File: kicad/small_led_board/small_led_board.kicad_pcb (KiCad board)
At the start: 2 copper layers, 137.2 x 99.1 mm, 107 parts, among them J1 Breakout to FPGA, J2 +5V IN, Q1 IRLZ44N, Q10 IRF4905, Q11 IRF4905, Q12 IRF4905, Q13 IRF4905, Q14 IRF4905, Q15 IRLZ44N, Q16 IRLZ44N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

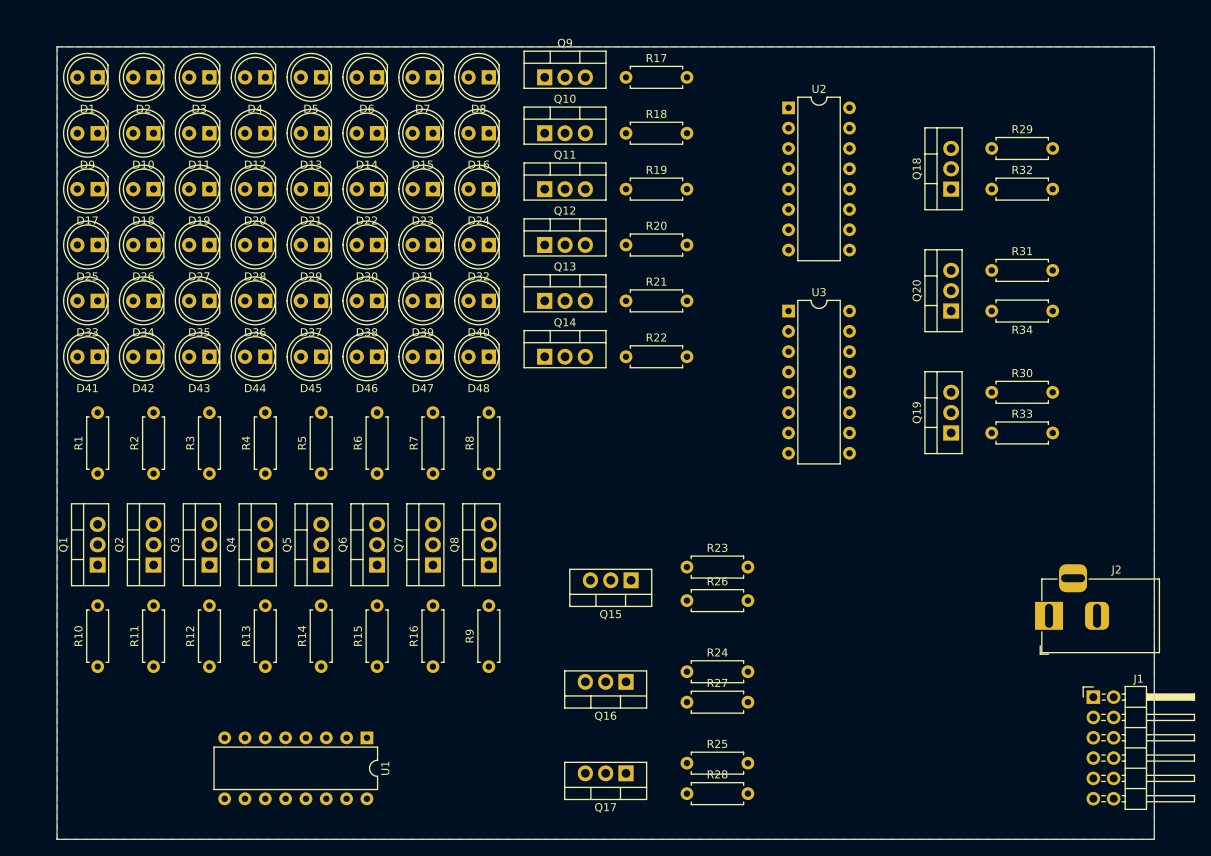
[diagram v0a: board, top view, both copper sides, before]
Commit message: small_led_board: Placed and Routed PCB
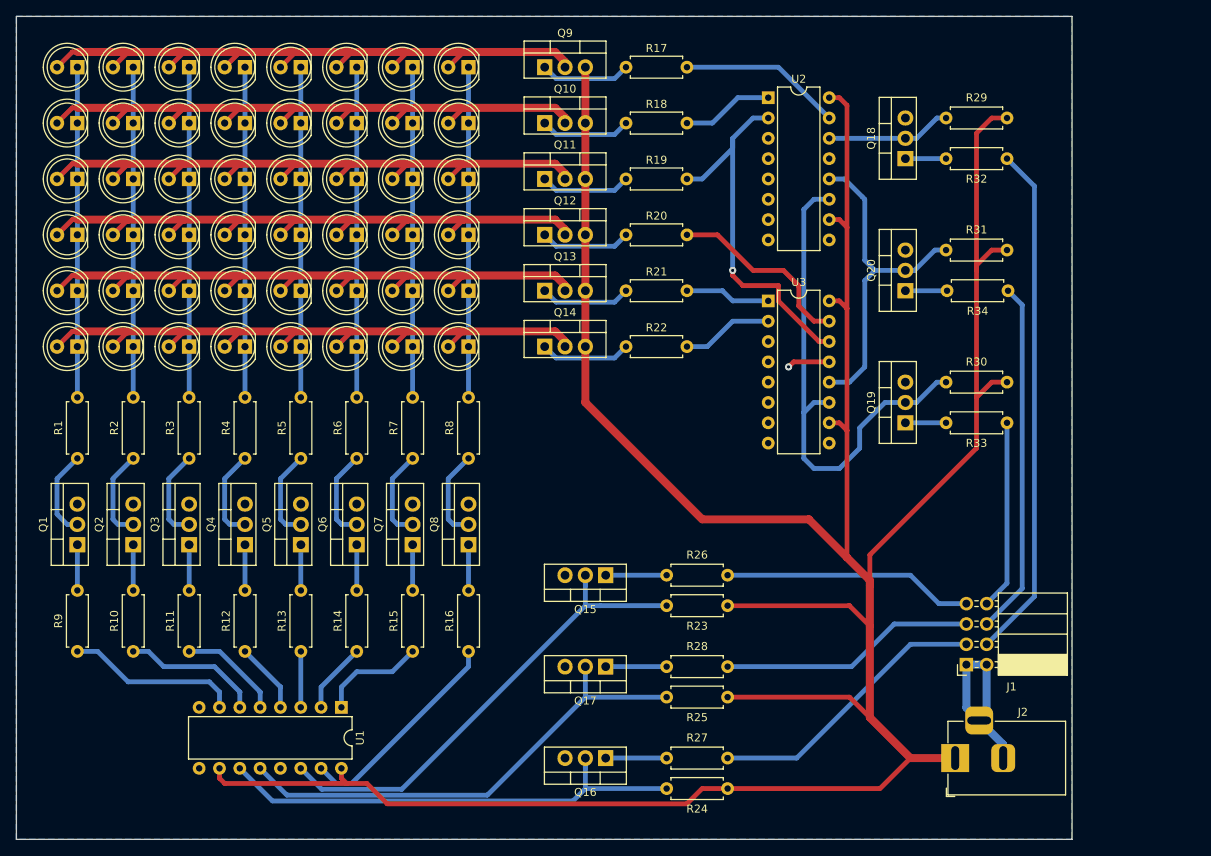
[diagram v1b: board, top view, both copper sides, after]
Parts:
- J1: value Breakout to FPGA -> TO FPGA; footprint Connector_PinHeader_2.54mm:PinHeader_2x06_P2.54mm_Horizontal -> Connector_PinSocket_2.54mm:PinSocket_2x04_P2.54mm_Horizontal
- moved R9 51.5 mm to (68.6, 116.2)
- moved J2 21.3 mm to (178.3, 129.5)
- moved J1 16.4 mm to (179.7, 117.9), turned to 180 degrees
- moved R28 16.1 mm to (142.2, 118.1)
- moved R24 14.8 mm to (142.2, 133.3)
- moved Q17 13.6 mm to (134.6, 118.1)
- moved R34 13.5 mm to (177.3, 71.1), turned to 0 degrees
- moved Q16 9.86 mm to (134.6, 129.5)
- moved R25 8.64 mm to (142.2, 121.9)
- moved R27 7.43 mm to (142.2, 129.5)
- moved Q18 6.87 mm to (172.1, 54.6)
- moved R29 6.87 mm to (177.2, 49.5)
- moved R32 6.87 mm to (177.2, 54.6)
- moved Q20 6.25 mm to (172.1, 71.1)
- moved R31 6.25 mm to (177.2, 66.0)
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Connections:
- J1 pad 1: FPGA_GND -> GND
- J1 pad 2: RowDataIn_n -> GND
- J1 pad 4: ApplyNewRow_n -> RowStrobeIn_n
- J1 pad 5: ApplyNewRowStrobe_n -> ApplyNewRow_n
- J1 pad 6: RowStrobeAdvance_n -> ApplyNewRowStrobe_n
- J1 pad 7: RowStrobeIn_n -> RowDataIn_n
- J1 pad 8: FPGA_GND -> RowStrobeAdvance_n
- J2 pad 1: GND -> +5V
- J2 pad 2: +5V -> GND
- J2 pad 3: (no net) -> GND
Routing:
- net +5V: track 0.00 -> 391.2 mm
- net Net-(D10-A): track 0.00 -> 84.4 mm
- net Net-(D33-A): track 0.00 -> 84.3 mm
- net Net-(D1-A): track 0.00 -> 84.3 mm
- net Net-(D17-A): track 0.00 -> 84.3 mm
- net Net-(D25-A): track 0.00 -> 84.3 mm
- net Net-(D41-A): track 0.00 -> 84.3 mm
- net RowStrobeIn_n: track 0.00 -> 64.6 mm
- net Net-(Q19-D): track 0.00 -> 62.8 mm
- net Net-(Q15-D): track 0.00 -> 61.4 mm
- net Net-(Q17-D): track 0.00 -> 61.1 mm
- net Net-(Q16-D): track 0.00 -> 60.8 mm
- net Net-(U2-QC): track 0.00 -> 47.8 mm, vias 0 -> 1
- net ApplyNewRowStrobe_n: track 0.00 -> 44.2 mm
- net Net-(Q20-D): track 0.00 -> 42.7 mm
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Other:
- board size 137.2 x 99.1 mm -> 132 x 102.9 mm
- copper layers 2 -> 4

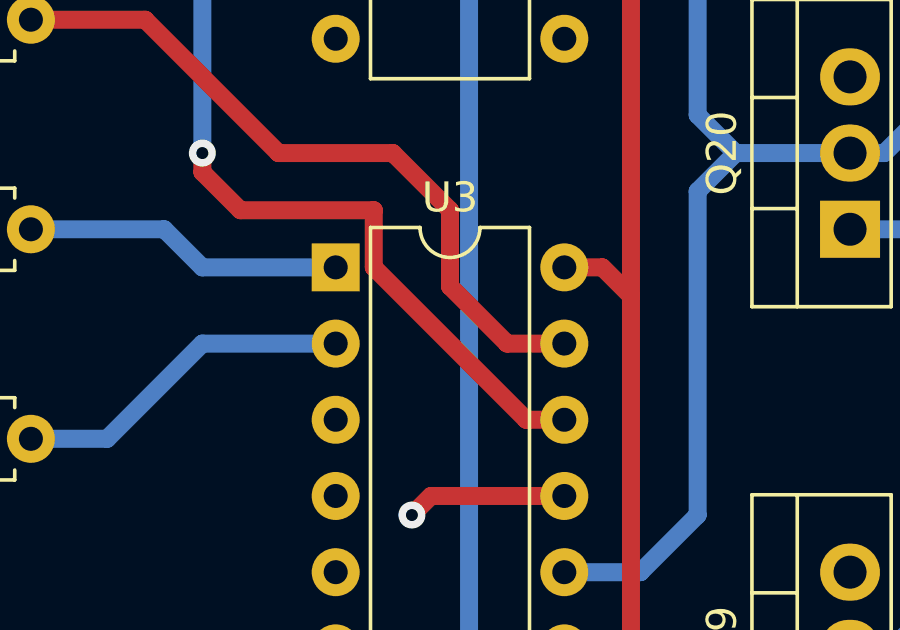
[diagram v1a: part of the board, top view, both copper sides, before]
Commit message: small_led_board: Changed PCB settings
Constraints were originally pulled from a git template project.
Changed 4 layers to 2 layers as only Front and Back are needed.
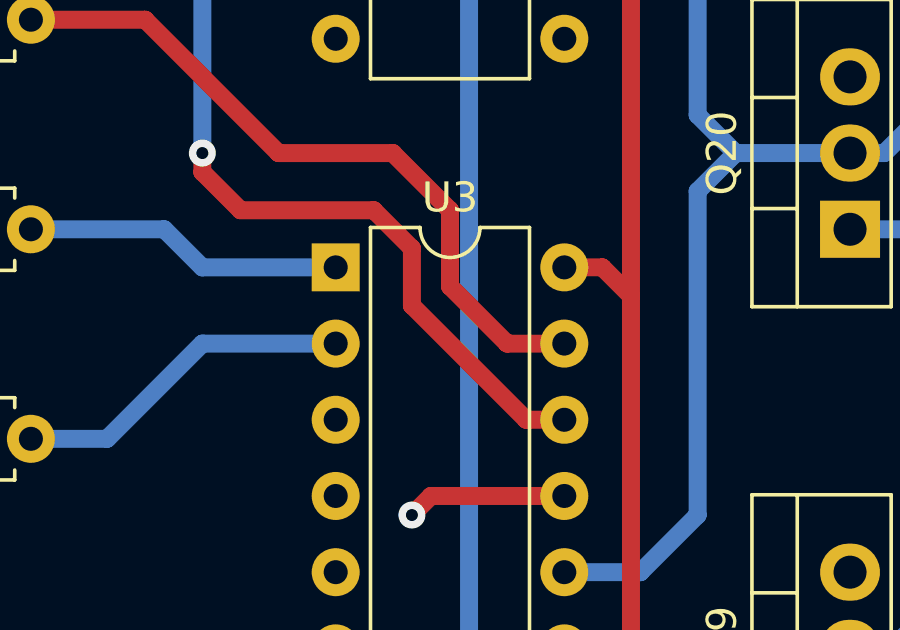
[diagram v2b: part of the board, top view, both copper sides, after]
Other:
- copper layers 4 -> 2
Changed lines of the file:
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@@
   (layers
     (0 "F.Cu" signal "Front")
-    (1 "In1.Cu" signal)
-    (2 "In2.Cu" signal)
     (31 "B.Cu" signal "Back")
     (34 "B.Paste" user)
@@
       (layer "F.Mask" (type "Top Solder Mask") (thickness 0.01))
       (layer "F.Cu" (type "copper") (thickness 0.035))
-      (layer "dielectric 1" (type "core") (thickness 1.51) (material "FR4") (epsilon_r 4.5) (loss_tangent 0.02))
-      (layer "In1.Cu" (type "copper") (thickness 0.035))
-      (layer "dielectric 2" (type "prepreg") (thickness 1.51) (material "FR4") (epsilon_r 4.5) (loss_tangent 0.02))
-      (layer "In2.Cu" (type "copper") (thickness 0.035))
-      (layer "dielectric 3" (type "core") (thickness 1.51) (material "FR4") (epsilon_r 4.5) (loss_tangent 0.02))
+      (layer "dielectric 1" (type "core") (thickness 4.6) (material "FR4") (epsilon_r 4.5) (loss_tangent 0.02))
       (layer "B.Cu" (type "copper") (thickness 0.035))
       (layer "B.Mask" (type "Bottom Solder Mask") (thickness 0.01))
@@
   (segment (start 144.78 50.165) (end 147.955 50.165) (width 0.6) (layer "B.Cu") (net 66))
   (segment (start 147.955 50.165) (end 151.13 46.99) (width 0.6) (layer "B.Cu") (net 66))
+  (segment (start 157.48 73.66) (end 157.48 71.755) (width 0.6) (layer "F.Cu") (net 67))
   (segment (start 156.21 70.485) (end 151.765 70.485) (width 0.6) (layer "F.Cu") (net 67))
-  (segment (start 156.21 72.39) (end 156.21 70.485) (width 0.6) (layer "F.Cu") (net 67))
-  (segment (start 151.765 70.485) (end 150.495 69.215) (width 0.6) (layer "F.Cu") (net 67))
   (segment (start 150.495 69.215) (end 150.495 68.58) (width 0.6) (layer "F.Cu") (net 67))
+  (segment (start 161.29 77.47) (end 157.48 73.66) (width 0.6) (layer "F.Cu") (net 67))
   (segment (start 162.56 77.47) (end 161.29 77.47) (width 0.6) (layer "F.Cu") (net 67))
-  (segment (start 161.29 77.47) (end 156.21 72.39) (width 0.6) (layer "F.Cu") (net 67))
+  (segment (start 157.48 71.755) (end 156.21 70.485) (width 0.6) (layer "F.Cu") (net 67))
+  (segment (start 151.765 70.485) (end 150.495 69.215) (width 0.6) (layer "F.Cu") (net 67))
   (via (at 150.495 68.58) (size 0.9) (drill 0.4) (layers "F.Cu" "B.Cu") (free) (net 67))
   (segment (start 144.78 57.15) (end 146.685 57.15) (width 0.6) (layer "B.Cu") (net 67))

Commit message: small_led_board: Renamed pin for more consistency
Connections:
- net RowStrobeAdvance_n renamed ShiftRowStrobe_n
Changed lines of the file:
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@@
   (net 17 "ApplyNewRow_n")
   (net 18 "ApplyNewRowStrobe_n")
-  (net 19 "RowStrobeAdvance_n")
+  (net 19 "ShiftRowStrobe_n")
   (net 20 "RowStrobeIn_n")
   (net 21 "Net-(Q1-G)")
@@
       (net 53 "Net-(Q19-G)") (pintype "passive"))
     (pad "2" thru_hole oval (at 7.62 0) (size 1.6 1.6) (drill 0.8) (layers "*.Cu" "*.Mask")
-      (net 19 "RowStrobeAdvance_n") (pintype "passive"))
+      (net 19 "ShiftRowStrobe_n") (pintype "passive"))
     (model "${KICAD6_3DMODEL_DIR}/Resistor_THT.3dshapes/R_Axial_DIN0207_L6.3mm_D2.5mm_P7.62mm_Horizontal.wrl"
       (offset (xyz 0 0 0))
@@
       (net 15 "RowDataIn_n") (pinfunction "Pin_7") (pintype "passive"))
     (pad "8" thru_hole oval (at -2.54 7.62 180) (size 1.7 1.7) (drill 1) (layers "*.Cu" "*.Mask")
-      (net 19 "RowStrobeAdvance_n") (pinfunction "Pin_8") (pintype "passive"))
+      (net 19 "ShiftRowStrobe_n") (pinfunction "Pin_8") (pintype "passive"))
     (model "${KICAD6_3DMODEL_DIR}/Connector_PinSocket_2.54mm.3dshapes/PinSocket_2x04_P2.54mm_Horizontal.wrl"
       (offset (xyz 0 0 0))

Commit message: kicad: updated resistor values to 1K
The small led board was barely managing to charge up the shift registers' lines with 10K without any additional strobing.
Now with this change in place, they can strobe four times easily. This is still not nearly the target we want to reach, but it's a first improvement.
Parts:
- R23, R24, R25, R29, R30, R31: value 10K -> 1K
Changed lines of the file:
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@@
         (effects (font (size 1 1) (thickness 0.15)))
     )
-    (fp_text value "10K" (at 3.81 2.37) (layer "F.Fab")
+    (fp_text value "1K" (at 3.81 2.37) (layer "F.Fab")
         (effects (font (size 1 1) (thickness 0.15)))
     )
@@
         (effects (font (size 1 1) (thickness 0.15)))
     )
-    (fp_text value "10K" (at 3.81 2.37) (layer "F.Fab")
+    (fp_text value "1K" (at 3.81 2.37) (layer "F.Fab")
         (effects (font (size 1 1) (thickness 0.15)))
     )
@@
         (effects (font (size 1 1) (thickness 0.15)))
     )
-    (fp_text value "10K" (at 3.81 2.37) (layer "F.Fab")
+    (fp_text value "1K" (at 3.81 2.37) (layer "F.Fab")
         (effects (font (size 1 1) (thickness 0.15)))
     )
@@
         (effects (font (size 1 1) (thickness 0.15)))
     )
-    (fp_text value "10K" (at 3.81 2.37) (layer "F.Fab")
+    (fp_text value "1K" (at 3.81 2.37) (layer "F.Fab")
         (effects (font (size 1 1) (thickness 0.15)))
     )
@@
         (effects (font (size 1 1) (thickness 0.15)))
     )
-    (fp_text value "10K" (at 3.81 2.37) (layer "F.Fab")
+    (fp_text value "1K" (at 3.81 2.37) (layer "F.Fab")
         (effects (font (size 1 1) (thickness 0.15)))
     )
@@
         (effects (font (size 1 1) (thickness 0.15)))
     )
-    (fp_text value "10K" (at 3.81 2.37) (layer "F.Fab")
+    (fp_text value "1K" (at 3.81 2.37) (layer "F.Fab")
         (effects (font (size 1 1) (thickness 0.15)))
     )
